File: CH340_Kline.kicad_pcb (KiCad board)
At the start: 2 copper layers, 36.7 x 18.9 mm, 10 parts, among them J1 Conn_01x06, J2 Conn_01x04, Q1 BC847, Q2 BC847

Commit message: routing complite
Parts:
- D1: value L9613 -> L9637D
- R1, R2, R3, R4: footprint Resistor_SMD:R_0805_2012Metric_Pad1.15x1.40mm_HandSolder -> Resistor_SMD:R_0805_2012Metric
- moved R4 14.4 mm to (90.9, 83.1), turned to 0 degrees
- moved R3 13.4 mm to (83.5, 83.1), turned to 180 degrees
- moved R2 9.47 mm to (94.5, 88.5)
- moved J2 6.74 mm to (101.5, 87.2)
- moved R1 6.21 mm to (83.5, 94.3)
- moved D2 6.06 mm to (99.4, 82.9)
- moved Q2 5.11 mm to (96.8, 94.1), turned to 0 degrees
- moved J1 4.65 mm to (77.1, 82.1)
- moved Q1 4.53 mm to (90.9, 94.1), turned to 90 degrees
- moved D1 3.21 mm to (85.6, 88.6)
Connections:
- D1 pad 3: Vcc -> 5V
- J1 pad 1: Rx -> 5V
- J1 pad 2: Tx -> 5V
- J1 pad 3: GND -> 3.3V
- J1 pad 4: 5V -> Tx
- J1 pad 5: Vcc -> Rx
- J1 pad 6: 3.3V -> GND
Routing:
- net K-line: track 0.00 -> 46.3 mm
- net Vss: track 0.00 -> 29.4 mm
- net GND: track 0.00 -> 28.0 mm
- net L-line: track 0.00 -> 25.9 mm
- net Tx: track 0.00 -> 19.7 mm
- net Rx: track 0.00 -> 14.1 mm
- net 5V: track 0.00 -> 10.2 mm
- net Net-(Q1-Pad3): track 0.00 -> 9.68 mm
- net Net-(Q1-Pad1): track 0.00 -> 5.64 mm
- net Net-(D2-Pad2): track 0.00 -> 4.39 mm
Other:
- board size 36.7 x 18.9 mm -> 28.7 x 17 mm
- net class Default: clearance 0.2 -> 0.15; trace_width 0.25 -> 0.7
- rule trace_clearance: 0.2 -> 0.15

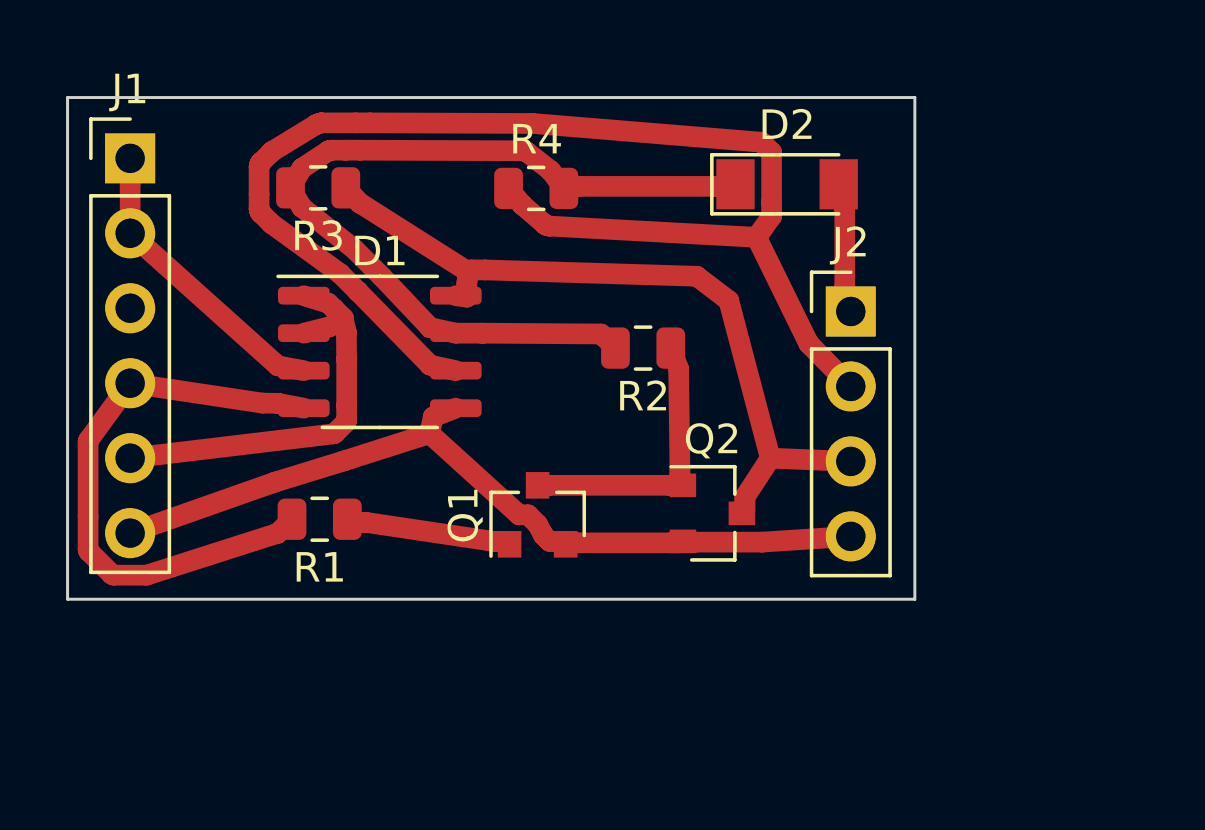
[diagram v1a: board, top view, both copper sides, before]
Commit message: add sym, add zone
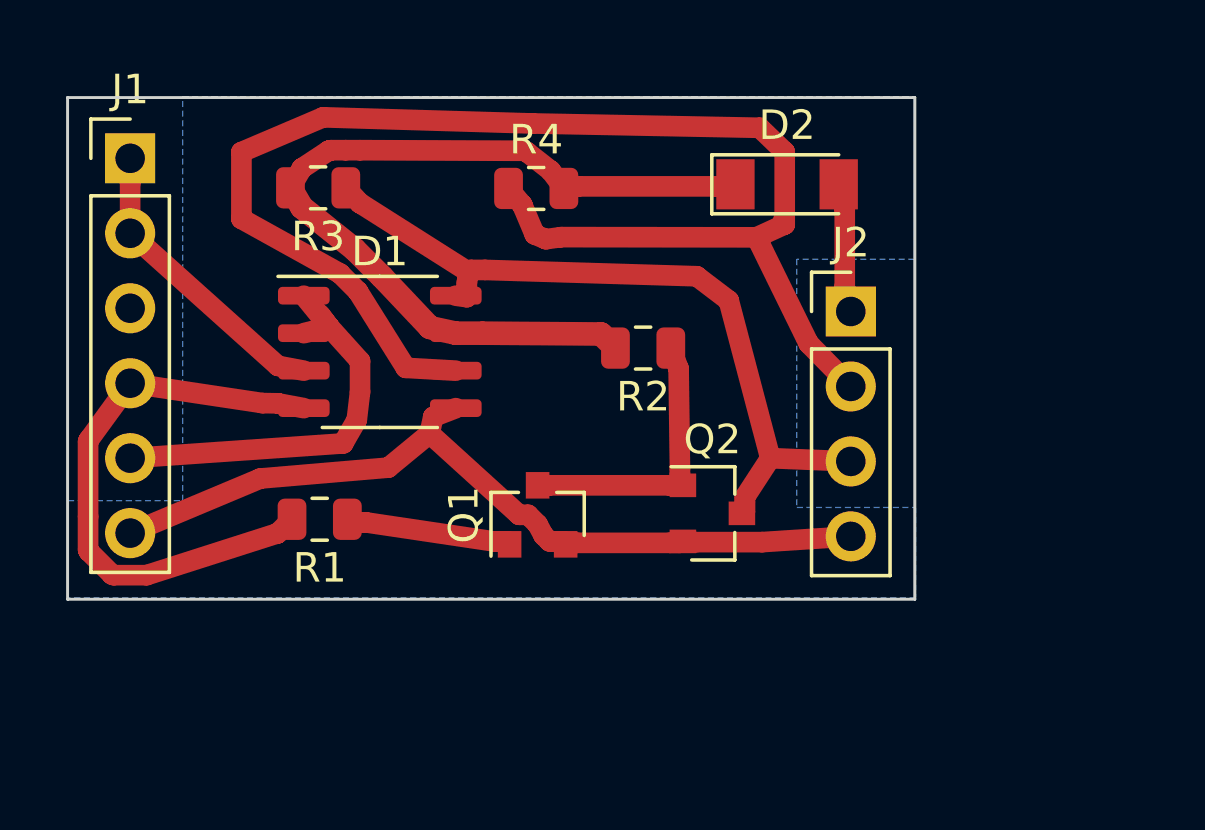
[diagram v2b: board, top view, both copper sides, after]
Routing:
- net K-line: track 46.3 -> 49.8 mm
- added copper zone on B.Cu, net GND
